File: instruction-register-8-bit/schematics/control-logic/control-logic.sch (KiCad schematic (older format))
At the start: 6 parts

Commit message: small corrections to design
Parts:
- removed U? (x2): 27C1024, symbol instruction-register-symbols:27C1024
- added U? (x2): 27C4096, symbol instruction-register-symbols:27C4096
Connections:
- net CF: now also U?.34 (A12), U?.34 (A12)
- net CL_1: now also U?.3 (Q15)
- net CL_10: now also U?.13 (Q6)
- net CL_11: now also U?.14 (Q5)
- net CL_12: now also U?.15 (Q4)
- net CL_2: now also U?.4 (Q14)
- net CL_28: now also U?.3 (Q15)
- net CL_29: now also U?.4 (Q14)
- net CL_3: now also U?.5 (Q13)
- net CL_30: now also U?.5 (Q13)
- net CL_31: now also U?.6 (Q12)
- net CL_32: now also U?.7 (Q11)
- net CL_33: now also U?.8 (Q10)
- net CL_34: now also U?.9 (Q9)
- net CL_35: now also U?.10 (Q8)
- net CL_36: now also U?.12 (Q7)
- net CL_37: now also U?.13 (Q6)
- net CL_38: now also U?.14 (Q5)
- net CL_39: now also U?.15 (Q4)
- net CL_4: now also U?.6 (Q12)
- net CL_5: now also U?.7 (Q11)
- net CL_6: now also U?.8 (Q10)
- net CL_7: now also U?.9 (Q9)
- net CL_8: now also U?.10 (Q8)
- net CL_9: now also U?.12 (Q7)
- net GND: now also U?.30 (Vss), U?.30 (Vss)
- net IR_0: now also U?.24 (A3), U?.24 (A3)
- net IR_1: now also U?.25 (A4), U?.25 (A4)
- net IR_2: now also U?.26 (A5), U?.26 (A5)
- net IR_3: now also U?.27 (A6), U?.27 (A6)
- net IR_4: now also U?.28 (A7), U?.28 (A7)
- net IR_5: now also U?.29 (A8), U?.29 (A8)
- net IR_6: now also U?.31 (A9), U?.31 (A9)
- net IR_7: now also U?.32 (A10), U?.32 (A10)
- net NF: now also U?.35 (A13), U?.35 (A13)
- net OF: now also U?.36 (A14), U?.36 (A14)
- net SC_0: now also U?.21 (A0), U?.21 (A0)
- net SC_1: now also U?.22 (A1), U?.22 (A1)
- net SC_2: now also U?.23 (A2), U?.23 (A2)
- net VCC: now also U?.1 (Vpp), U?.1 (Vpp), U?.39 (A17), U?.40 (Vcc), U?.40 (Vcc)
- net ZF: now also U?.33 (A11), U?.33 (A11)
- net at U?.4 (~E1), U?.6 (E3): now also U?.16 (Q3) (x2)
- net at U?.3 (A2), U?.3 (A2): now also U?.17 (Q2) (x2)
- net at U?.2 (A1), U?.2 (A1): now also U?.18 (Q1) (x2)
- net at U?.1 (AO), U?.1 (AO): now also U?.19 (Q0) (x2)
- new net: U?.11 (Vss), U?.2 (~CE), U?.20 (~OE), U?.37 (A15), U?.38 (A16)
- new net: U?.11 (Vss), U?.2 (~CE), U?.20 (~OE), U?.37 (A15), U?.38 (A16), U?.39 (A17)
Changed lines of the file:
@@
 $EndDescr
-$Comp
-L instruction-register-symbols:27C1024 U?
-U 1 1 60D31697
-P 3925 2975
-F 0 "U?" V 4725 3050 50  0000 C CNN
-F 1 "27C1024" V 4325 1425 50  0000 C CNN
-F 2 "" H 4000 2900 50  0001 C CNN
-F 3 "" H 4000 2900 50  0001 C CNN
-	1    3925 2975
-	0    1    1    0
-$EndComp
 $Comp
 L instruction-register-symbols:74HCT238 U?
@@
 CL_27
 $Comp
-L instruction-register-symbols:27C1024 U?
-U 1 1 60E15E62
-P 8900 2975
-F 0 "U?" V 9700 3050 50  0000 C CNN
-F 1 "27C1024" V 9325 1425 50  0000 C CNN
-F 2 "" H 8975 2900 50  0001 C CNN
-F 3 "" H 8975 2900 50  0001 C CNN
-	1    8900 2975
-	0    1    1    0
-$EndComp
-$Comp
 L instruction-register-symbols:74HCT238 U?
 U 1 1 60E15E68
@@
 Text HLabel 9325 6150 3    50   Input ~ 0
 CL_54
-Wire Wire Line
-	1475 3325 1475 3475
 $Comp
 L power:GND #PWR?
@@
 	1    0    0    -1
 $EndComp
-Connection ~ 1475 3475
 $Comp
 L power:GND #PWR?
@@
 Connection ~ 2325 1900
 Wire Wire Line
-	1900 2875 1900 2800
-Wire Wire Line
-	1900 2800 1775 2800
-Wire Wire Line
-	1475 2800 1475 3325
-Connection ~ 1475 3325
-Wire Wire Line
-	1775 2875 1775 2800
-Connection ~ 1775 2800
-Wire Wire Line
-	1775 2800 1475 2800
-Wire Wire Line
-	2025 2875 2025 2800
-Wire Wire Line
-	2025 2800 2225 2800
-Wire Wire Line
-	4175 2800 4175 3325
+	4175 2725 4175 3325
 Wire Wire Line
 	4175 3475 4025 3475
@@
 $EndComp
 Wire Wire Line
-	7000 2750 9150 2750
-Wire Wire Line
-	9150 2750 9150 3325
-Wire Wire Line
 	9150 3475 9000 3475
 Wire Wire Line
@@
 $EndComp
 Wire Wire Line
-	7000 2750 7000 2875
-Wire Wire Line
-	2225 2875 2225 2800
-Connection ~ 2225 2800
-Wire Wire Line
-	2225 2800 4175 2800
-Wire Wire Line
-	6450 3325 6450 2800
-Wire Wire Line
-	6450 2800 6750 2800
+	6450 2800 6650 2800
 Wire Wire Line
 	6750 2800 6750 2875
-Wire Wire Line
-	6750 2800 6875 2800
-Wire Wire Line
-	6875 2800 6875 2875
 Connection ~ 6750 2800
 Wire Wire Line
 	7200 2875 7200 2800
-Wire Wire Line
-	7200 2800 6875 2800
-Connection ~ 6875 2800
 $Comp
 L power:GND #PWR?
@@
 Text Notes 1375 6975 0    79   ~ 0
 All control lines should be each be connected to an LED and current\nlimiting resistor combo as an indicator of the control line being HIGH.
-Wire Wire Line
-	6450 3325 6450 3475
-Connection ~ 6450 3325
 $Comp
 L power:GND #PWR?
@@
 	1    0    0    -1
 $EndComp
-Connection ~ 6450 3475
 Text Notes 1575 3925 0    59   ~ 0
 LEFT
 Text Notes 6550 3925 0    59   ~ 0
 RIGHT
+Wire Wire Line
+	1475 2800 1475 3325
+$Comp
+L instruction-register-symbols:27C4096 U?
+U 1 1 60DAC648
+P 3925 2975
+F 0 "U?" V 4700 3000 50  0000 L CNN
+F 1 "27C4096" V 4325 1625 50  0000 L CNN
+F 2 "" H 4000 2900 50  0001 C CNN
+F 3 "" H 4000 2900 50  0001 C CNN
+	1    3925 2975
+	0    1    1    0
+$EndComp
+Wire Wire Line
+	1475 2800 1675 2800
+Wire Wire Line
+	1675 2800 1675 2875
+Wire Wire Line
+	1675 2800 1775 2800
+Wire Wire Line
+	1775 2800 1775 2875
+Connection ~ 1675 2800
+Connection ~ 1775 2800
+Wire Wire Line
+	2125 2800 2125 2875
+Wire Wire Line
+	6450 2800 6450 3325
+$Comp
+L instruction-register-symbols:27C4096 U?
+U 1 1 60E3BD23
+P 8900 2975
+F 0 "U?" V 9675 3000 50  0000 L CNN
+F 1 "27C4096" V 9300 1625 50  0000 L CNN
+F 2 "" H 8975 2900 50  0001 C CNN
+F 3 "" H 8975 2900 50  0001 C CNN
+	1    8900 2975
+	0    1    1    0
+$EndComp
+Wire Wire Line
+	6750 2800 7000 2800
+Wire Wire Line
+	7100 2875 7100 2800
+Connection ~ 7100 2800
+Wire Wire Line
+	7100 2800 7200 2800
+Wire Wire Line
+	7000 2875 7000 2800
+Connection ~ 7000 2800
+Wire Wire Line
+	7000 2800 7100 2800
+Wire Wire Line
+	6650 2875 6650 2800
+Connection ~ 6650 2800
+Wire Wire Line
+	6650 2800 6750 2800
+Wire Wire Line
+	1775 2800 2125 2800
+Wire Wire Line
+	2025 2725 2025 2875
+Wire Wire Line
+	2025 2725 4175 2725
+Wire Wire Line
+	2125 2800 2225 2800
+Wire Wire Line
+	2225 2800 2225 2875
+Connection ~ 2125 2800
 $EndSCHEMATC

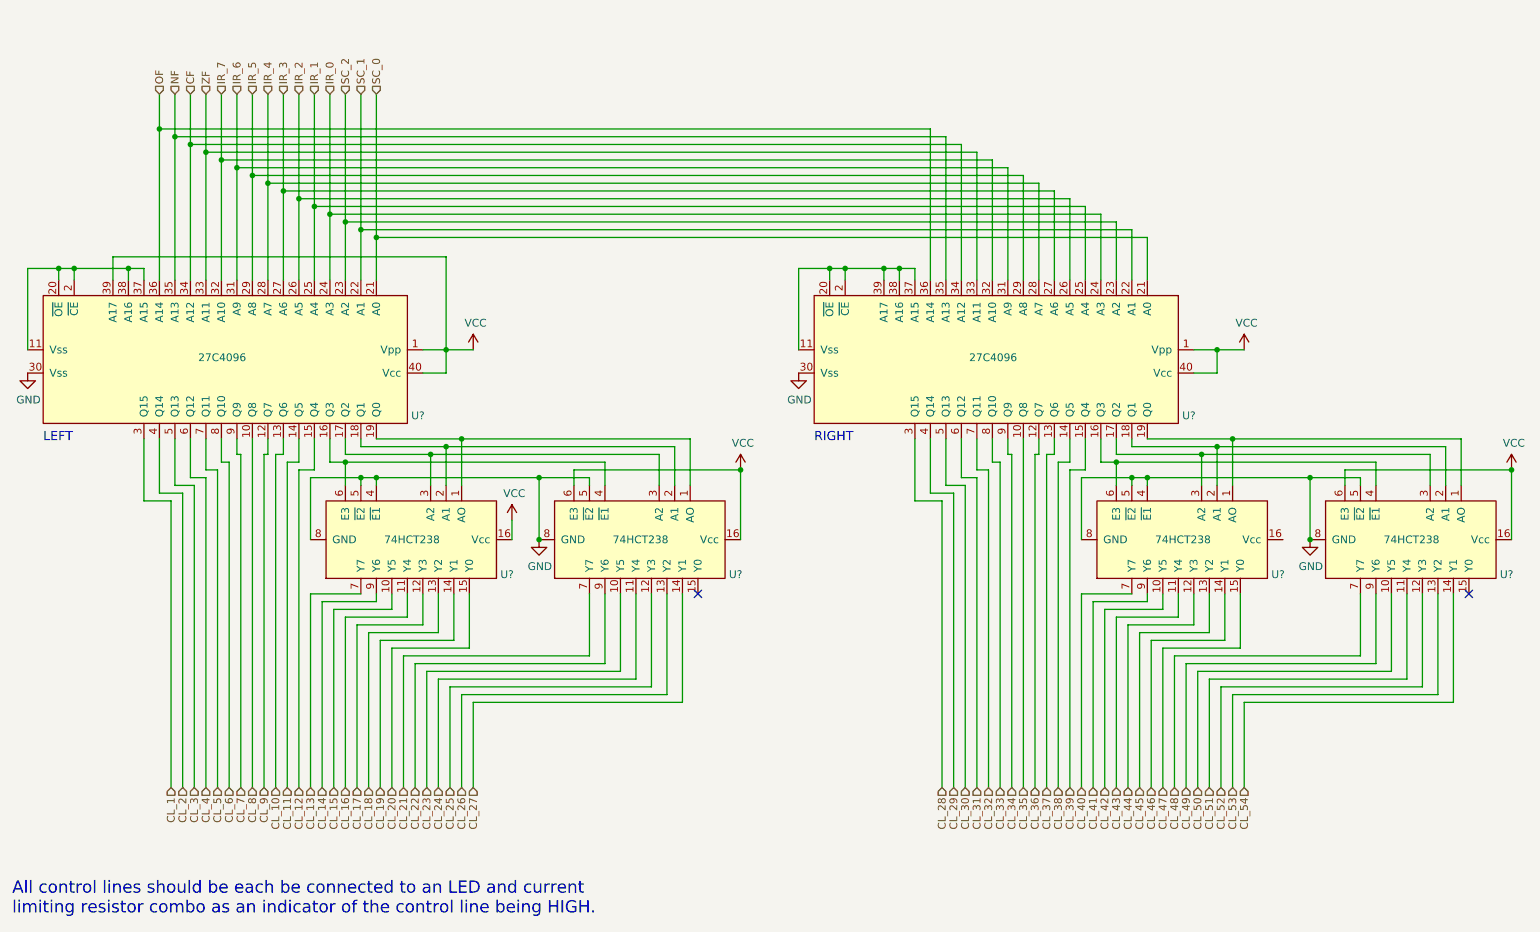
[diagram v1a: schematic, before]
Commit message: updated register design to enable extended instructions
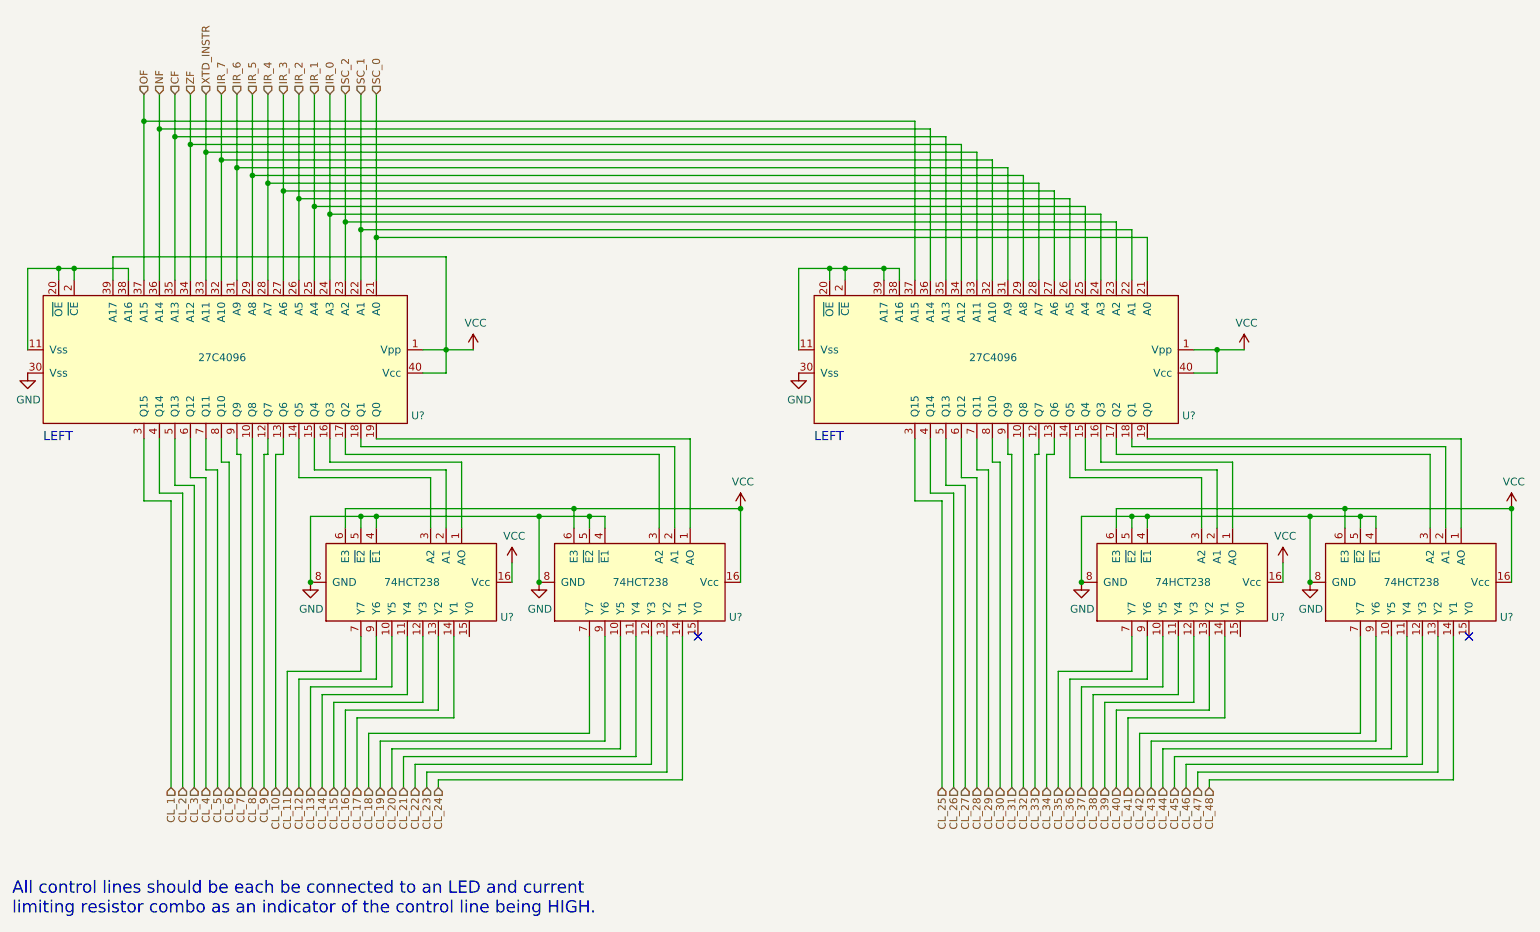
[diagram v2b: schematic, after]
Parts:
- removed U? (x2): 74HCT238, symbol instruction-register-symbols:74HCT238
- removed U?: 27C4096, symbol instruction-register-symbols:27C4096
- added U? (x2): 74HCT238, symbol instruction-register-symbols:74HCT238
- added U?: 27C4096, symbol instruction-register-symbols:27C4096
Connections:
- net CF: now also U?.35 (A13), U?.35 (A13); no longer U?.34 (A12)
- net CL_11: now also U?.7 (Y7); no longer U?.14 (Q5)
- net CL_12: now also U?.9 (Y6); no longer U?.15 (Q4)
- net CL_13: now also U?.10 (Y5); no longer U?.7 (Y7)
- net CL_14: now also U?.11 (Y4); no longer U?.9 (Y6)
- net CL_15: now also U?.12 (Y3); no longer U?.10 (Y5)
- net CL_16: now also U?.13 (Y2); no longer U?.11 (Y4)
- net CL_17: now also U?.14 (Y1); no longer U?.12 (Y3)
- net CL_18: now also U?.7 (Y7); no longer U?.13 (Y2)
- net CL_19: now also U?.9 (Y6); no longer U?.14 (Y1)
- net CL_20: now also U?.10 (Y5); no longer U?.15 (Y0)
- net CL_21: now also U?.11 (Y4); no longer U?.7 (Y7)
- net CL_22: now also U?.12 (Y3); no longer U?.9 (Y6)
- net CL_23: now also U?.13 (Y2); no longer U?.10 (Y5)
- net CL_24: now also U?.14 (Y1); no longer U?.11 (Y4)
- net CL_25: now also U?.3 (Q15); no longer U?.12 (Y3)
- net CL_26: now also U?.4 (Q14); no longer U?.13 (Y2)
- net CL_27: now also U?.5 (Q13); no longer U?.14 (Y1)
- net CL_28: now also U?.6 (Q12)
- net CL_29: now also U?.7 (Q11)
- net CL_30: now also U?.8 (Q10)
- net CL_31: now also U?.9 (Q9)
- net CL_32: now also U?.10 (Q8)
- net CL_33: now also U?.12 (Q7)
- net CL_34: now also U?.13 (Q6)
- net CL_35: now also U?.7 (Y7)
- net CL_36: now also U?.9 (Y6)
- net CL_37: now also U?.10 (Y5)
- net CL_38: now also U?.11 (Y4)
- net CL_39: now also U?.12 (Y3)
- net CL_40: now also U?.13 (Y2)
- net CL_41: now also U?.14 (Y1)
- net CL_42: now also U?.7 (Y7)
- net CL_43: now also U?.9 (Y6)
- net CL_44: now also U?.10 (Y5)
- net CL_45: now also U?.11 (Y4)
- net CL_46: now also U?.12 (Y3)
- net CL_47: now also U?.13 (Y2)
- net CL_48: now also U?.14 (Y1)
- net GND: now also U?.4 (~E1), U?.30 (Vss), U?.4 (~E1), U?.4 (~E1), U?.5 (~E2), U?.5 (~E2), U?.8 (GND), U?.8 (GND)
- net IR_0: now also U?.24 (A3)
- net IR_1: now also U?.25 (A4)
- net IR_2: now also U?.26 (A5)
- net IR_3: now also U?.27 (A6)
- net IR_4: now also U?.28 (A7)
- net IR_5: now also U?.29 (A8)
- net IR_6: now also U?.31 (A9)
- net IR_7: now also U?.32 (A10)
- net NF: now also U?.36 (A14), U?.36 (A14); no longer U?.35 (A13)
- net OF: now also U?.37 (A15), U?.37 (A15); no longer U?.36 (A14)
- net SC_0: now also U?.21 (A0)
- net SC_1: now also U?.22 (A1)
- net SC_2: now also U?.23 (A2)
- net VCC: now also U?.6 (E3), U?.1 (Vpp), U?.16 (Vcc), U?.16 (Vcc), U?.40 (Vcc), U?.6 (E3), U?.6 (E3)
- net ZF: now also U?.34 (A12), U?.34 (A12); no longer U?.33 (A11)
- net at U?.1 (AO), U?.19 (Q0): no longer U?.1 (AO)
- net at U?.18 (Q1), U?.2 (A1): no longer U?.2 (A1)
- net at U?.17 (Q2), U?.3 (A2): no longer U?.3 (A2)
- net at U?.11 (Vss), U?.2 (~CE), U?.20 (~OE)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: no longer U?.37 (A15)
- new net: U?.1 (AO), U?.16 (Q3) (x2)
- new net: U?.15 (Q4), U?.2 (A1) (x2)
- new net: U?.14 (Q5), U?.3 (A2) (x2)
- new net: U?.1 (AO), U?.19 (Q0)
- new net: U?.18 (Q1), U?.2 (A1)
- new net: U?.17 (Q2), U?.3 (A2)
- new net: U?.11 (Vss), U?.2 (~CE), U?.20 (~OE), U?.38 (A16), U?.39 (A17)
- new net XTD_INSTR: U?.33 (A11), U?.33 (A11)
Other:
- note removed: "RIGHT"
- moved on the sheet: U?

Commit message: candidate final schematic designs
Also started to consolidate custom symbols from all projects
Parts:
- U? (x4): symbol instruction-register-symbols:74HCT238 -> common-symbols:74HCT238
- U? (x2): symbol instruction-register-symbols:27C4096 -> common-symbols:27C4096
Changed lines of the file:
@@
 $EndDescr
 $Comp
-L instruction-register-symbols:74HCT238 U?
+L common-symbols:74HCT238 U?
 U 1 1 60DA7B46
 P 5450 4825
@@
 $EndComp
 $Comp
-L instruction-register-symbols:74HCT238 U?
+L common-symbols:74HCT238 U?
 U 1 1 60D8B240
 P 3975 4825
@@
 	1475 2800 1475 3325
 $Comp
-L instruction-register-symbols:27C4096 U?
+L common-symbols:27C4096 U?
 U 1 1 60DAC648
 P 3925 2975
@@
 	3600 5700 4225 5700
 $Comp
-L instruction-register-symbols:74HCT238 U?
+L common-symbols:74HCT238 U?
 U 1 1 61437C3F
 P 10425 4825
@@
 $EndComp
 $Comp
-L instruction-register-symbols:74HCT238 U?
+L common-symbols:74HCT238 U?
 U 1 1 61437C45
 P 8950 4825
@@
 	6450 2800 6450 3325
 $Comp
-L instruction-register-symbols:27C4096 U?
+L common-symbols:27C4096 U?
 U 1 1 61437CC3
 P 8900 2975
